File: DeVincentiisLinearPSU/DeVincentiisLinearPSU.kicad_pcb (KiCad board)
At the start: 2 copper layers, 93 x 101 mm, 129 parts, among them J1 0-12-24Vac, J10 V_set, J11 A_set, J2 UPDI, J3 0-24V, J4 Fan 24V, J5 +POW, J6 TP1, J7 +OUT, J8 -POW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

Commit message: Value of R49 changed to 330K ohms because with transformers with slightly higher voltage the current limiter had difficulty lowering the output voltage
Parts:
- R49: value 150K -> 330K
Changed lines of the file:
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@@
 			)
 		)
-		(property "Value" "150K"
+		(property "Value" "330K"
 			(at 0 -1.82 90)
 			(layer "B.Fab")

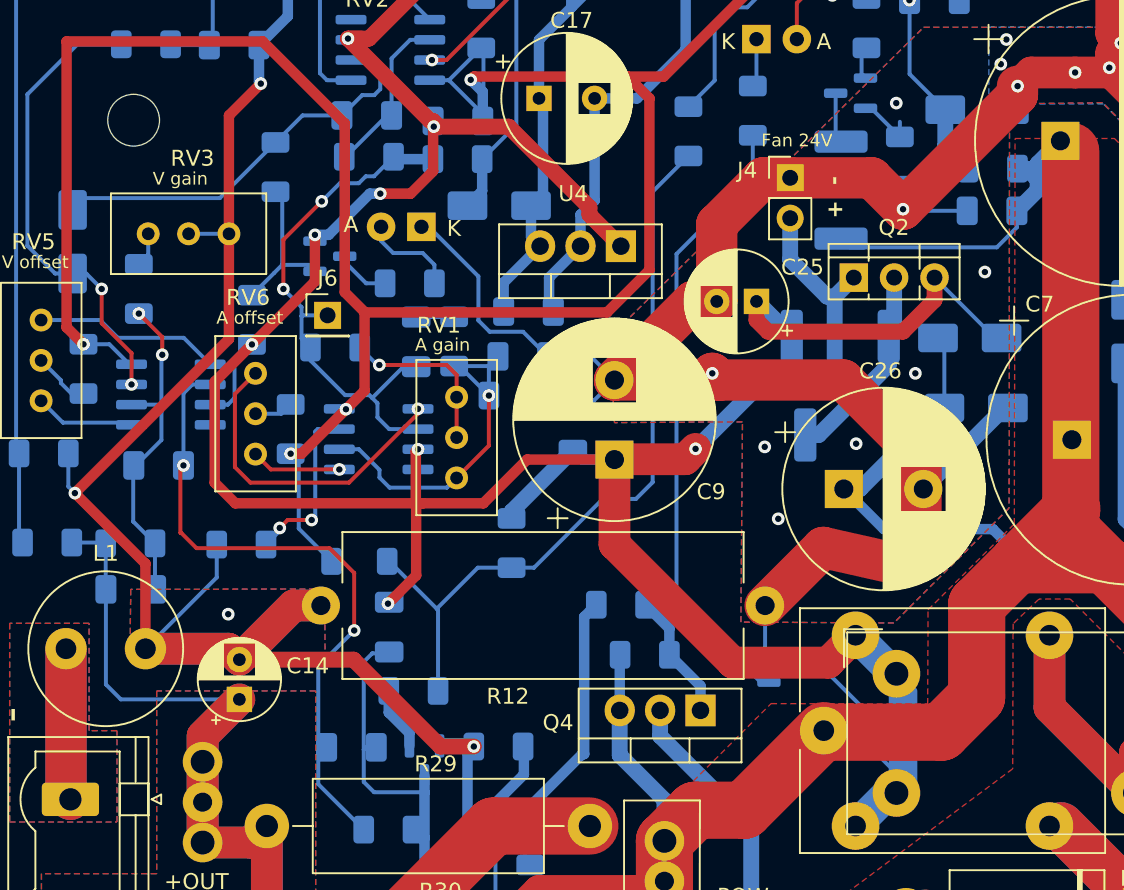
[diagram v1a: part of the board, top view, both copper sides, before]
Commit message: I change the mode for self-oscillation prevention by increasing the capacitance of C18 which now works as both integrator/low-pass. Firmware fixed too
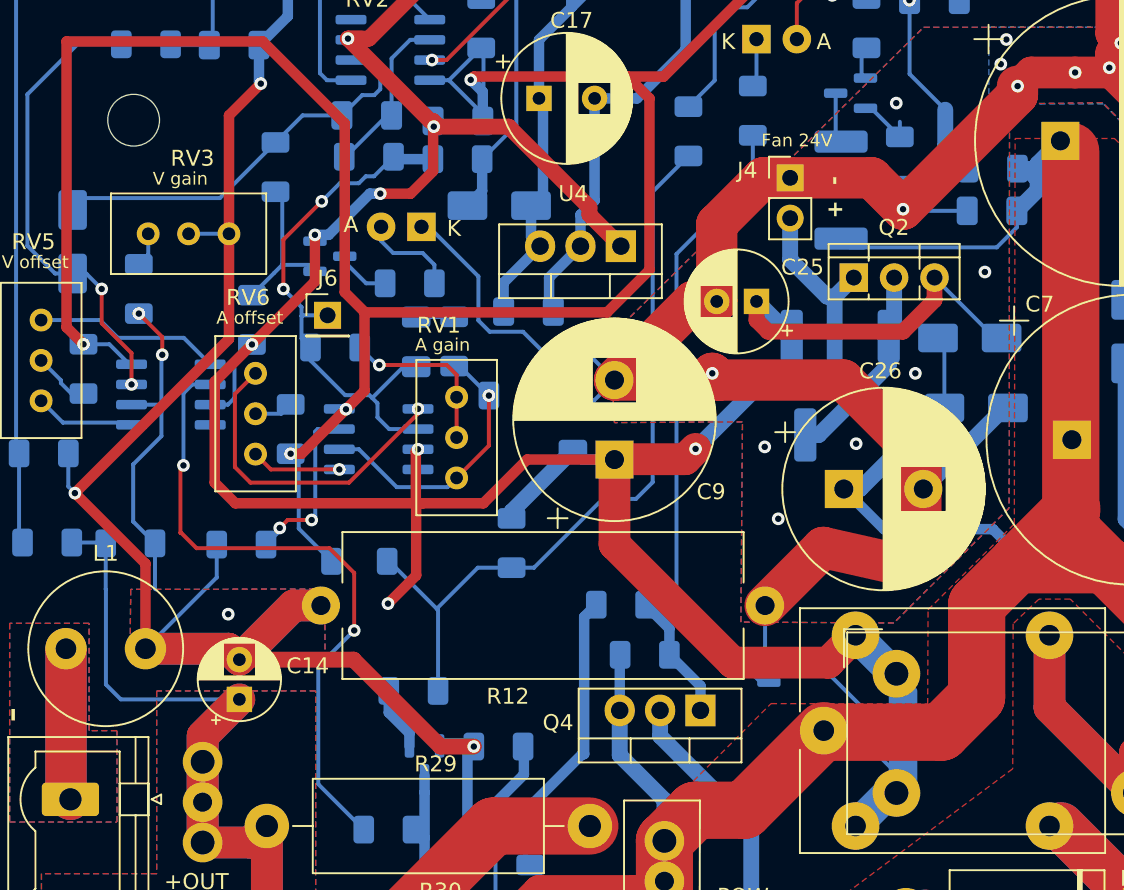
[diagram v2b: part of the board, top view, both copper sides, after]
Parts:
- removed C19: 100p, Capacitor_SMD:C_1206_3216Metric_Pad1.33x1.80mm_HandSolder
- removed C20, C22: 330p, Capacitor_SMD:C_1206_3216Metric_Pad1.33x1.80mm_HandSolder
- removed C24: 470p, Capacitor_SMD:C_1206_3216Metric_Pad1.33x1.80mm_HandSolder
- removed C28: 0p, Capacitor_SMD:C_1206_3216Metric_Pad1.33x1.80mm_HandSolder
- removed D7: 4.7V, Diode_SMD:D_SMA
- C18: value 470p -> 10n
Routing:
- net Net-(Q5-B): track 35.1 -> 20.9 mm
- net Net-(U2--): track 23.6 -> 17.6 mm

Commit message: Fixed PCB errors. Replace C19 and added R51 to prevent self-oscillations
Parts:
- added C19: 1n, Capacitor_SMD:C_1206_3216Metric_Pad1.33x1.80mm_HandSolder, B.Cu at (89.4, 99.1)
- added R51: 1000, Resistor_SMD:R_1206_3216Metric_Pad1.30x1.75mm_HandSolder, B.Cu at (85.8, 100.6)
- R49: value 330K -> 220K
- moved J11 3.25 mm to (115.2, 52.6)
- turned R23 to 180 degrees
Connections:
- R23 pad 1: Net-(R23-Pad1) -> Net-(Q5-B)
- R23 pad 2: Net-(Q5-B) -> Net-(C19-Pad2)
- U7 pad 6: Net-(R23-Pad1) -> Net-(C19-Pad2)
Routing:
- net Net-(C19-Pad2): track 0.00 -> 43.4 mm, vias 0 -> 2
- net Net-(R23-Pad1): track 41.0 -> 0.00 mm, vias 2 -> 0
- net /+24V: track 175.3 -> 168.2 mm, vias 9 -> 8
- net /A_SET: track 11.4 -> 15.8 mm
- net /-V out: track 366.3 -> 370.1 mm
- net Net-(U7--): track 21.6 -> 18.7 mm
- net Net-(C19-Pad1): track 0.00 -> 2.08 mm

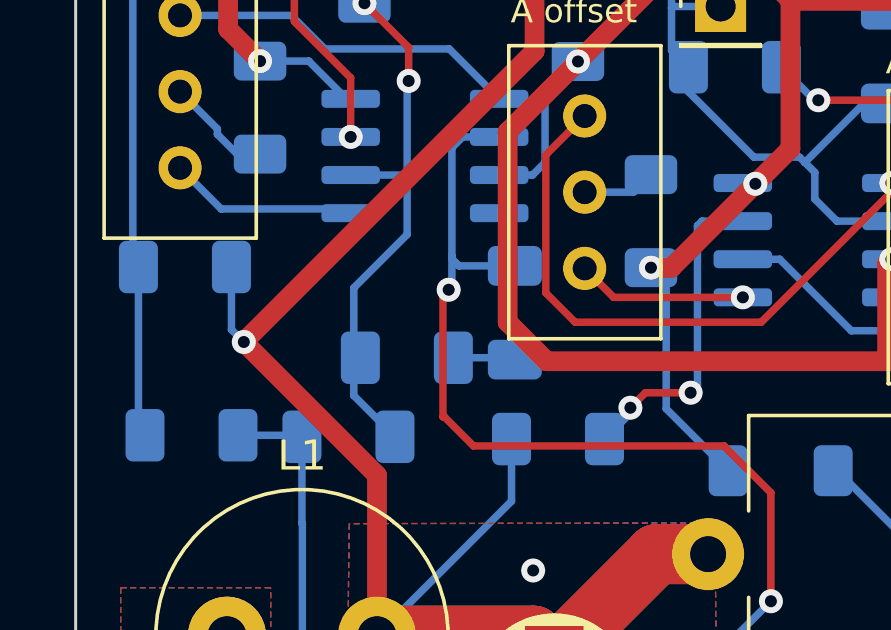
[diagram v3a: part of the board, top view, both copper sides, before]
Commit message: C19 and R51 removed
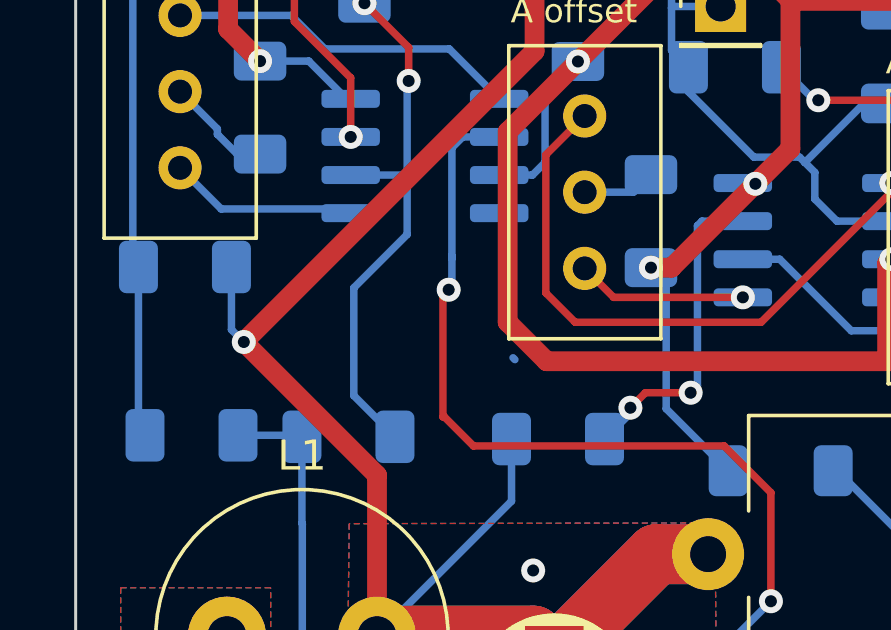
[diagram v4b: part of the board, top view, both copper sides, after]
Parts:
- removed C19: 1n, Capacitor_SMD:C_1206_3216Metric_Pad1.33x1.80mm_HandSolder
- removed R51: 1000, Resistor_SMD:R_1206_3216Metric_Pad1.30x1.75mm_HandSolder
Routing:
- net Net-(R23-Pad2): track 43.4 -> 41.2 mm
- net Net-(C19-Pad1): track 2.08 -> 0.00 mm

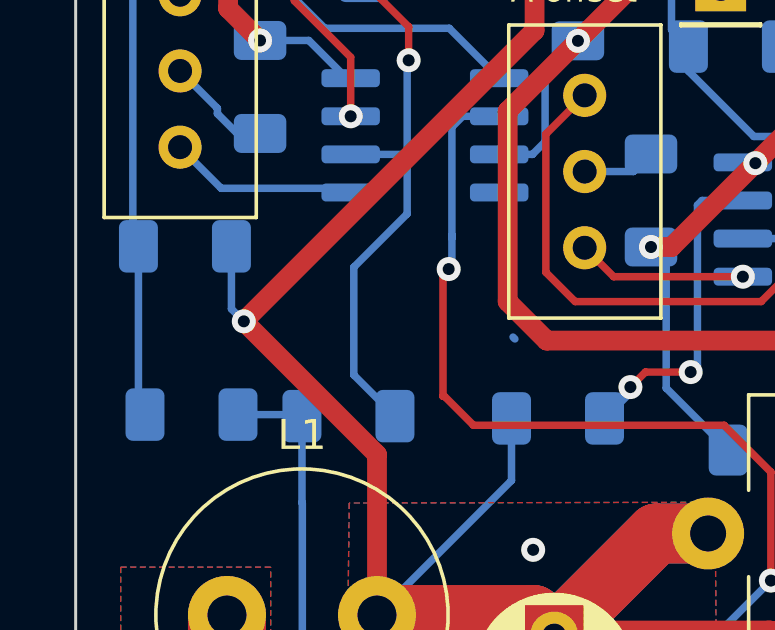
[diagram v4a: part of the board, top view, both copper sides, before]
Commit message: C22 reverted for improve and/or personalize self-oscillations immunity. Added parametric Freecad electronic enclosure
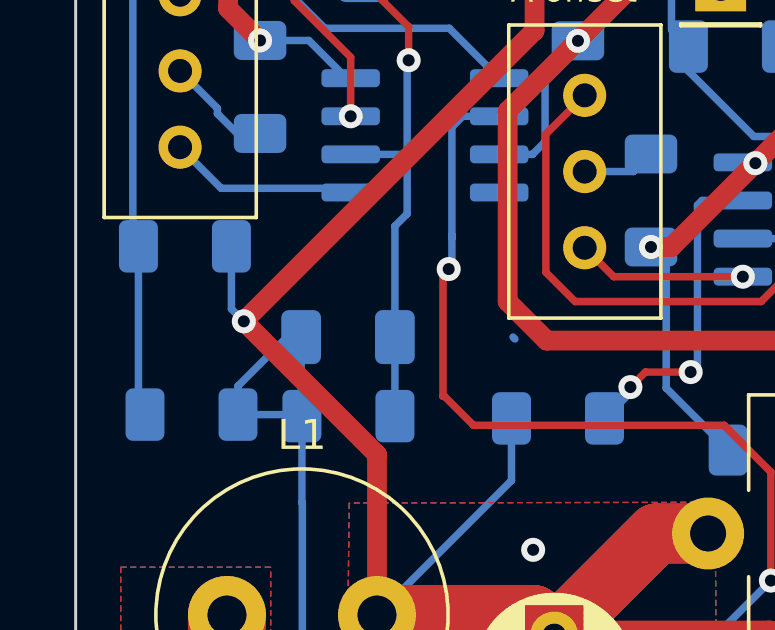
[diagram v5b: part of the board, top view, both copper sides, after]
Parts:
- added C22: 330p, Capacitor_SMD:C_1206_3216Metric_Pad1.33x1.80mm_HandSolder, B.Cu at (83.8, 100.6)
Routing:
- net /+V out: track 67.2 -> 73.6 mm
- net Net-(U7--): track 18.7 -> 17.6 mm
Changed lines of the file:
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@@
 		(tags "resistor handsolder")
 		(property "Reference" "R45"
-			(at 0.3284 1.7948 180)
+			(at 0 -1.98901 180)
 			(layer "B.SilkS")
 			(effects
@@
 		(tags "resistor handsolder")
 		(property "Reference" "R28"
-			(at 0.3434 1.9686 180)
+			(at 0 -1.96521 180)
 			(layer "B.SilkS")
 			(effects
@@
 		)
 	)
+	(footprint "Capacitor_SMD:C_1206_3216Metric_Pad1.33x1.80mm_HandSolder"
+		(layer "B.Cu")
+		(at 83.8375 100.6 180)
+		(descr "Capacitor SMD 1206 (3216 Metric), square (rectangular) end terminal, IPC_7351 nominal with elongated pad for handsoldering. (Body size source: IPC-SM-782 page 76, https://www.pcb-3d.com/wordpress/wp-content/uploads/ipc-sm-782a_amendment_1_and_2.pdf), generated with kicad-footprint-generator")
+		(tags "capacitor handsolder")
+		(property "Reference" "C22"
+			(at 0 1.85 0)
+			(layer "B.SilkS")
+			(effects
+				(font
+					(size 1 1)
+					(thickness 0.15)
+				)
+				(justify mirror)
+			)
+		)
+		(property "Value" "330p"
+			(at 0 -1.85 0)
+			(layer "B.Fab")
+			(effects
+				(font
+					(size 1 1)
+					(thickness 0.15)
+				)
+				(justify mirror)
+			)
+		)
+		(property "Datasheet" ""
+			(at 0 0 0)
+			(unlocked yes)
+			(layer "B.Fab")
+			(hide yes)
+			(effects
+				(font
+					(size 1.27 1.27)
+					(thickness 0.15)
+				)
+				(justify mirror)
+			)
+		)
+		(property "Description" ""
+			(at 0 0 0)
+			(unlocked yes)
+			(layer "B.Fab")
+			(hide yes)
+			(effects
+				(font
+					(size 1.27 1.27)
+					(thickness 0.15)
+				)
+				(justify mirror)
+			)
+		)
+		(property ki_fp_filters "C_*")
+		(sheetname "/")
+		(sheetfile "DeVincentiisLinearPSU.kicad_sch")
+		(attr smd)
+		(fp_line
+			(start -0.711252 0.91)
+			(end 0.711252 0.91)
+			(stroke
+				(width 0.12)
+				(type solid)
+			)
+			(layer "B.SilkS")
+		)
+		(fp_line
+			(start -0.711252 -0.91)
+			(end 0.711252 -0.91)
+			(stroke
+				(width 0.12)
+				(type solid)
+			)
+			(layer "B.SilkS")
+		)
+		(fp_line
+			(start 2.48 1.15)
+			(end 2.48 -1.15)
+			(stroke
+				(width 0.05)
+				(type solid)
+			)
+			(layer "B.CrtYd")
+		)
+		(fp_line
+			(start 2.48 -1.15)
+			(end -2.48 -1.15)
+			(stroke
+				(width 0.05)
+				(type solid)
+			)
+			(layer "B.CrtYd")
+		)
+		(fp_line
+			(start -2.48 1.15)
+			(end 2.48 1.15)
+			(stroke
+				(width 0.05)
+				(type solid)
+			)
+			(layer "B.CrtYd")
+		)
+		(fp_line
+			(start -2.48 -1.15)
+			(end -2.48 1.15)
+			(stroke
+				(width 0.05)
+				(type solid)
+			)
+			(layer "B.CrtYd")
+		)
+		(fp_line
+			(start 1.6 0.8)
+			(end 1.6 -0.8)
+			(stroke
+				(width 0.1)
+				(type solid)
+			)
+			(layer "B.Fab")
+		)
+		(fp_line
+			(start 1.6 -0.8)
+			(end -1.6 -0.8)
+			(stroke
+				(width 0.1)
+				(type solid)
+			)
+			(layer "B.Fab")
+		)
+		(fp_line
+			(start -1.6 0.8)
+			(end 1.6 0.8)
+			(stroke
+				(width 0.1)
+				(type solid)
+			)
+			(layer "B.Fab")
+		)
+		(fp_line
+			(start -1.6 -0.8)
+			(end -1.6 0.8)
+			(stroke
+				(width 0.1)
+				(type solid)
+			)
+			(layer "B.Fab")
+		)
+		(fp_text user "${REFERENCE}"
+			(at 0 0 0)
+			(layer "B.Fab")
+			(effects
+				(font
+					(size 0.8 0.8)
+					(thickness 0.12)
+				)
+				(justify mirror)
+			)
+		)
+		(pad "1" smd roundrect
+			(at -1.5625 0 180)
+			(size 1.325 1.8)
+			(layers "B.Cu" "B.Mask" "B.Paste")
+			(roundrect_rratio 0.188679)
+			(net 29 "Net-(U7--)")
+			(pintype "passive")
+		)
+		(pad "2" smd roundrect
+			(at 1.5625 0 180)
+			(size 1.325 1.8)
+			(layers "B.Cu" "B.Mask" "B.Paste")
+			(roundrect_rratio 0.188679)
+			(net 17 "/+V out")
+			(pintype "passive")
+		)
+		(embedded_fonts no)
+		(model "${KICAD9_3DMODEL_DIR}/Capacitor_SMD.3dshapes/C_1206_3216Metric.wrl"
+			(offset
+				(xyz 0 0 0)
+			)
+			(scale
+				(xyz 1 1 1)
+			)
+			(rotate
+				(xyz 0 0 0)
+			)
+		)
+	)
 	(footprint "Package_SO:SOIC-20W_7.5x12.8mm_P1.27mm"
 		(layer "B.Cu")
@@
 	)
 	(segment
+		(start 82.275 103.20758)
+		(end 82.30221 103.23479)
+		(width 0.25)
+		(layer "B.Cu")
+		(net 17)
+	)
+	(segment
 		(start 88.39881 116.97619)
 		(end 88.39881 122.05619)
@@
 	)
 	(segment
+		(start 82.275 100.6)
+		(end 81.8 100.6)
+		(width 0.25)
+		(layer "B.Cu")
+		(net 17)
+	)
+	(segment
+		(start 81.8 100.6)
+		(end 80.16981 102.23019)
+		(width 0.25)
+		(layer "B.Cu")
+		(net 17)
+	)
+	(segment
 		(start 82.31511 106.13039)
 		(end 82.31511 112.11169)
@@
 	)
 	(segment
+		(start 82.275 100.6)
+		(end 82.275 103.20758)
+		(width 0.25)
+		(layer "B.Cu")
+		(net 17)
+	)
+	(segment
 		(start 92.43881 128.91619)
 		(end 95.00881 128.91619)
@@
 	)
 	(segment
+		(start 80.16981 102.23019)
+		(end 80.16981 103.18399)
+		(width 0.25)
+		(layer "B.Cu")
+		(net 17)
+	)
+	(segment
 		(start 88.39881 116.97619)
 		(end 88.39881 115.361903)
@@
 	(segment
 		(start 85.80801 96.49199)
-		(end 84.03001 98.26999)
+		(end 85.4 96.9)
 		(width 0.25)
 		(layer "B.Cu")
@@
 	)
 	(segment
-		(start 84.03001 101.86259)
-		(end 85.40221 103.23479)
+		(start 85.4 96.9)
+		(end 85.4 103.23258)
 		(width 0.25)
 		(layer "B.Cu")
@@
 	)
 	(segment
-		(start 85.85881 91.37299)
-		(end 85.80801 91.42379)
+		(start 85.80801 94.92899)
+		(end 85.80801 96.49199)
 		(width 0.25)
 		(layer "B.Cu")
@@
 	)
 	(segment
-		(start 85.80801 94.92899)
-		(end 85.80801 96.49199)
+		(start 85.85881 91.37299)
+		(end 85.80801 91.42379)
 		(width 0.25)
 		(layer "B.Cu")
@@
 	)
 	(segment
-		(start 84.03001 98.26999)
-		(end 84.03001 101.86259)
+		(start 85.4 103.23258)
+		(end 85.40221 103.23479)
 		(width 0.25)
 		(layer "B.Cu")

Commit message: Added R51
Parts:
- added R51: 1000, Resistor_SMD:R_1206_3216Metric_Pad1.30x1.75mm_HandSolder, B.Cu at (84.8, 99.4)
- C22: value 330p -> 10n
- moved C22 1.87 mm to (82.4, 99.4), turned to 90 degrees
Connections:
- C22 pad 1: Net-(U7--) -> /+V out
- C22 pad 2: /+V out -> Net-(C22-Pad2)
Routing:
- net Net-(C22-Pad2): track 0.00 -> 2.41 mm
- net Net-(U7--): track 17.6 -> 19.5 mm

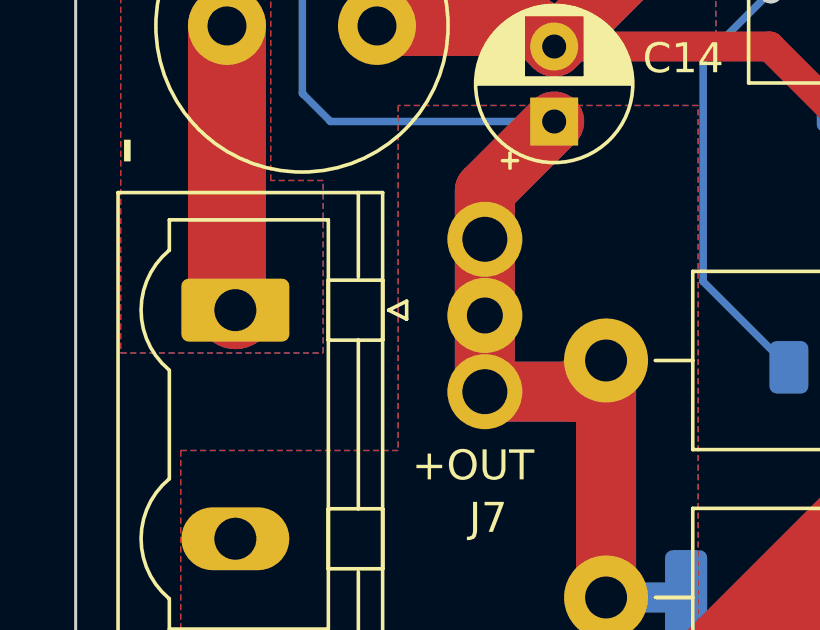
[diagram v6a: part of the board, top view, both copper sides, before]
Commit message: DigitalLinearPowerSupply: added C19 (snubber)
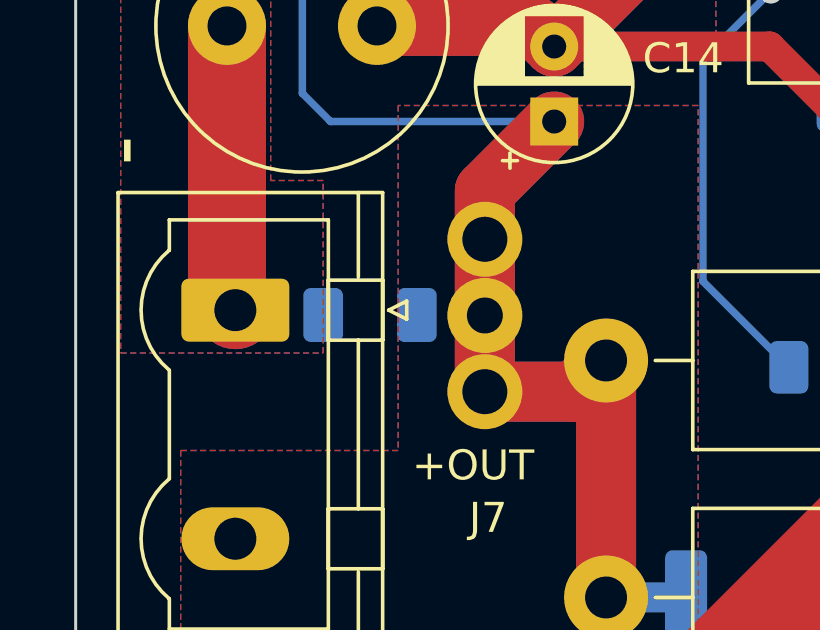
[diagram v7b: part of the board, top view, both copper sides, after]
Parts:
- added C19: 470n, Capacitor_SMD:C_1206_3216Metric_Pad1.33x1.80mm_HandSolder, B.Cu at (84.6, 119.5)
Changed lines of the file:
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@@
 	(title_block
 		(title "DeVincentiisDigitalLinearPSU")
-		(date "2024-05-31")
-		(rev "4.4")
+		(date "2025-05-29")
+		(rev "4.5")
 		(company "ADVisor Antonio De Vincentiis")
 		(comment 1 "https://devincentiis.it")
@@
 			(offset
 				(xyz 0 0 0)
+			)
+			(scale
+				(xyz 1 1 1)
+			)
+			(rotate
+				(xyz 0 0 0)
+			)
+		)
+	)
+	(footprint "Capacitor_SMD:C_1206_3216Metric_Pad1.33x1.80mm_HandSolder"
+		(layer "B.Cu")
+		(at 84.57131 119.5 180)
+		(descr "Capacitor SMD 1206 (3216 Metric), square (rectangular) end terminal, IPC_7351 nominal with elongated pad for handsoldering. (Body size source: IPC-SM-782 page 76, https://www.pcb-3d.com/wordpress/wp-content/uploads/ipc-sm-782a_amendment_1_and_2.pdf), generated with kicad-footprint-generator")
+		(tags "capacitor handsolder")
+		(property "Reference" "C19"
+			(at 0 1.85 0)
+			(layer "B.SilkS")
+			(effects
+				(font
+					(size 1 1)
+					(thickness 0.15)
+				)
+				(justify mirror)
+			)
+		)
+		(property "Value" "470n"
+			(at 0 -1.85 0)
+			(layer "B.Fab")
+			(effects
+				(font
+					(size 1 1)
+					(thickness 0.15)
+				)
+				(justify mirror)
+			)
+		)
+		(property "Datasheet" ""
+			(at 0 0 0)
+			(unlocked yes)
+			(layer "B.Fab")
+			(hide yes)
+			(effects
+				(font
+					(size 1.27 1.27)
+					(thickness 0.15)
+				)
+				(justify mirror)
+			)
+		)
+		(property "Description" ""
+			(at 0 0 0)
+			(unlocked yes)
+			(layer "B.Fab")
+			(hide yes)
+			(effects
+				(font
+					(size 1.27 1.27)
+					(thickness 0.15)
+				)
+				(justify mirror)
+			)
+		)
+		(property ki_fp_filters "C_*")
+		(sheetname "/")
+		(sheetfile "DeVincentiisLinearPSU.kicad_sch")
+		(attr smd)
+		(fp_line
+			(start -0.711252 0.91)
+			(end 0.711252 0.91)
+			(stroke
+				(width 0.12)
+				(type solid)
+			)
+			(layer "B.SilkS")
+		)
+		(fp_line
+			(start -0.711252 -0.91)
+			(end 0.711252 -0.91)
+			(stroke
+				(width 0.12)
+				(type solid)
+			)
+			(layer "B.SilkS")
+		)
+		(fp_line
+			(start 2.48 1.15)
+			(end 2.48 -1.15)
+			(stroke
+				(width 0.05)
+				(type solid)
+			)
+			(layer "B.CrtYd")
+		)
+		(fp_line
+			(start 2.48 -1.15)
+			(end -2.48 -1.15)
+			(stroke
+				(width 0.05)
+				(type solid)
+			)
+			(layer "B.CrtYd")
+		)
+		(fp_line
+			(start -2.48 1.15)
+			(end 2.48 1.15)
+			(stroke
+				(width 0.05)
+				(type solid)
+			)
+			(layer "B.CrtYd")
+		)
+		(fp_line
+			(start -2.48 -1.15)
+			(end -2.48 1.15)
+			(stroke
+				(width 0.05)
+				(type solid)
+			)
+			(layer "B.CrtYd")
+		)
+		(fp_line
+			(start 1.6 0.8)
+			(end 1.6 -0.8)
+			(stroke
+				(width 0.1)
+				(type solid)
+			)
+			(layer "B.Fab")
+		)
+		(fp_line
+			(start 1.6 -0.8)
+			(end -1.6 -0.8)
+			(stroke
+				(width 0.1)
+				(type solid)
+			)
+			(layer "B.Fab")
+		)
+		(fp_line
+			(start -1.6 0.8)
+			(end 1.6 0.8)
+			(stroke
+				(width 0.1)
+				(type solid)
+			)
+			(layer "B.Fab")
+		)
+		(fp_line
+			(start -1.6 -0.8)
+			(end -1.6 0.8)
+			(stroke
+				(width 0.1)
+				(type solid)
+			)
+			(layer "B.Fab")
+		)
+		(fp_text user "${REFERENCE}"
+			(at 0 0 0)
+			(layer "B.Fab")
+			(effects
+				(font
+					(size 0.8 0.8)
+					(thickness 0.12)
+				)
+				(justify mirror)
+			)
+		)
+		(pad "1" smd roundrect
+			(at -1.5625 0 180)
+			(size 1.325 1.8)
+			(layers "B.Cu" "B.Mask" "B.Paste")
+			(roundrect_rratio 0.188679)
+			(net 17 "/+V out")
+			(pintype "passive")
+		)
+		(pad "2" smd roundrect
+			(at 1.5625 0 180)
+			(size 1.325 1.8)
+			(layers "B.Cu" "B.Mask" "B.Paste")
+			(roundrect_rratio 0.188679)
+			(net 68 "Net-(J3-Pin_1)")
+			(pintype "passive")
+		)
+		(embedded_fonts no)
+		(model "${KICAD9_3DMODEL_DIR}/Capacitor_SMD.3dshapes/C_1206_3216Metric.wrl"
+			(offset
+				(xyz 0 0 0)
